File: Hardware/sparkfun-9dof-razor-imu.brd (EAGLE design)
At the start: 31.8 x 31.8 mm, 57 parts, among them J1 LiPo, J3 USD_CONNECTOR, U1 3.3V, U2 MCP73831, U3 MPU-9250, U4 ATSAMD21G-A, Y1 32.768kHz

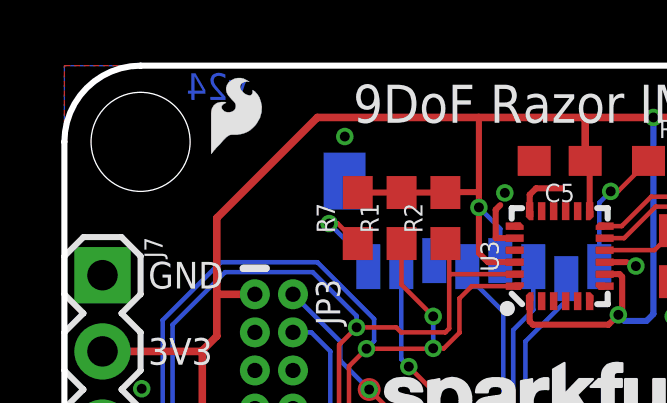
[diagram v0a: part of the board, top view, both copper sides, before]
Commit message: Updating version number to redboard release - v30
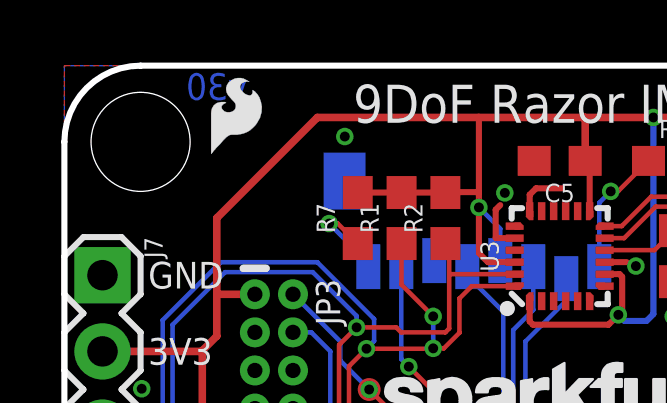
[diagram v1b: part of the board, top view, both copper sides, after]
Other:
- board text added: "v30"
- board text removed: "v24"
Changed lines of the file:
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@@
 <setting verticaltext="up"/>
 </settings>
-<grid distance="0.05" unitdist="inch" unit="inch" style="lines" multiple="1" display="yes" altdistance="0.0025" altunitdist="inch" altunit="inch"/>
+<grid distance="0.05" unitdist="inch" unit="inch" style="lines" multiple="1" display="yes" altdistance="0.005" altunitdist="inch" altunit="inch"/>
 <layers>
 <layer number="1" name="Top" color="4" fill="1" visible="yes" active="yes"/>
@@
 <text x="5.08" y="19.685" size="0.889" layer="22" font="vector" ratio="15" rot="MR0" align="center-left">SDA</text>
 <text x="5.08" y="17.145" size="0.889" layer="22" font="vector" ratio="15" rot="MR0" align="center-left">SCL</text>
-<text x="5.08" y="31.496" size="0.889" layer="16" font="vector" ratio="15" rot="MR180" align="bottom-center">v24</text>
+<text x="5.08" y="31.496" size="0.889" layer="16" font="vector" ratio="15" rot="MR180" align="bottom-center">v30</text>
 <text x="0.254" y="13.97" size="0.889" layer="22" font="vector" ratio="15" rot="MR90" align="bottom-center">ON</text>
 <text x="0.254" y="7.62" size="0.889" layer="22" font="vector" ratio="15" rot="MR90" align="bottom-center">OFF</text>

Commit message: Post-review changes - swapping 3.3V and GND, moving switch in.
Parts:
- moved S1 0.13 mm to (2.92, 10.9)
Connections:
- net 3.3V: now also J5.7; no longer J5.8
- net GND: now also J5.8; no longer J5.7
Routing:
- net 3.3V: track 121.0 -> 123.5 mm
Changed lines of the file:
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@@
 <setting verticaltext="up"/>
 </settings>
-<grid distance="0.05" unitdist="inch" unit="inch" style="lines" multiple="1" display="yes" altdistance="0.005" altunitdist="inch" altunit="inch"/>
+<grid distance="0.05" unitdist="inch" unit="inch" style="lines" multiple="1" display="yes" altdistance="0.001" altunitdist="inch" altunit="inch"/>
 <layers>
 <layer number="1" name="Top" color="4" fill="1" visible="yes" active="yes"/>
@@
 <text x="25.019" y="7.493" size="1.778" layer="22" font="vector" ratio="15" rot="MR0">+</text>
 <text x="20.193" y="7.493" size="1.778" layer="22" font="vector" ratio="15" rot="MR0">-</text>
-<text x="29.0195" y="22.225" size="0.889" layer="21" font="vector" ratio="15" rot="R90" align="bottom-center">GND</text>
-<text x="29.0195" y="24.765" size="0.889" layer="21" font="vector" ratio="15" rot="R90" align="bottom-center">3V3</text>
-<text x="24.13" y="12.065" size="0.889" layer="21" font="vector" ratio="15" align="center-right">A0</text>
+<text x="29.0195" y="24.765" size="0.889" layer="21" font="vector" ratio="15" rot="R90" align="bottom-center">GND</text>
+<text x="29.0195" y="22.225" size="0.889" layer="21" font="vector" ratio="15" rot="R90" align="bottom-center">3V3</text>
+<text x="24.13" y="12.065" size="0.8636" layer="21" font="vector" ratio="15" align="center-right">A0</text>
 <text x="24.13" y="14.605" size="0.889" layer="21" font="vector" ratio="15" align="center-right">A1</text>
 <text x="24.13" y="17.145" size="0.889" layer="21" font="vector" ratio="15" align="center-right">A2</text>
@@
 <text x="20.32" y="2.794" size="0.889" layer="21" font="vector" ratio="15" align="bottom-center">GND</text>
 <text x="23.622" y="2.794" size="0.889" layer="21" font="vector" ratio="15" align="bottom-center">VBAT</text>
-<text x="29.21" y="24.765" size="0.889" layer="22" font="vector" ratio="15" rot="MR270" align="bottom-center">3V3</text>
-<text x="29.21" y="22.225" size="0.889" layer="22" font="vector" ratio="15" rot="MR270" align="bottom-center">GND</text>
+<text x="29.21" y="22.225" size="0.889" layer="22" font="vector" ratio="15" rot="MR270" align="bottom-center">3V3</text>
+<text x="29.21" y="24.765" size="0.889" layer="22" font="vector" ratio="15" rot="MR270" align="bottom-center">GND</text>
 <text x="29.21" y="19.685" size="0.889" layer="22" font="vector" ratio="15" rot="MR270" align="bottom-center">RX</text>
 <text x="29.21" y="17.145" size="0.889" layer="22" font="vector" ratio="15" rot="MR270" align="bottom-center">TX</text>
@@
 <element name="H4" library="SparkFun-Electromechanical" package="STAND-OFF" value="STAND-OFF" x="2.54" y="29.21"/>
 <element name="H3" library="SparkFun-Electromechanical" package="STAND-OFF" value="STAND-OFF" x="29.21" y="29.21"/>
-<element name="S1" library="SparkFun-Electromechanical" package="SWITCH-SPST-SMD-A" value="" x="2.794" y="10.922" rot="MR270">
-<attribute name="PROD_ID" value="SWCH-10651" x="2.794" y="10.922" size="1.778" layer="28" font="vector" ratio="15" rot="MR270" display="off"/>
+<element name="S1" library="SparkFun-Electromechanical" package="SWITCH-SPST-SMD-A" value="" x="2.921" y="10.922" rot="MR270">
+<attribute name="PROD_ID" value="SWCH-10651" x="2.921" y="10.922" size="1.778" layer="28" font="vector" ratio="15" rot="MR270" display="off"/>
 </element>
 <element name="R6" library="SparkFun-Resistors" package="0603" value="100k" x="20.32" y="28.575">
@@
 <via x="5.6261" y="15.2654" extent="1-16" drill="0.3302"/>
 <via x="12.192" y="12.5222" extent="1-16" drill="0.3302"/>
-<contactref element="J5" pad="7"/>
 <via x="22.1996" y="14.6431" extent="1-16" drill="0.3302"/>
 <via x="18.2626" y="13.4874" extent="1-16" drill="0.3302"/>
@@
 <wire x1="18.1864" y1="15.2146" x2="18.7198" y2="15.748" width="0.2032" layer="1"/>
 <wire x1="18.7198" y1="15.748" x2="19.304" y2="15.748" width="0.2032" layer="1"/>
+<contactref element="J5" pad="8"/>
 </signal>
 <signal name="REGOUT">
@@
 <wire x1="4.5974" y1="22.2504" x2="5.08" y2="22.733" width="0.254" layer="1"/>
 <wire x1="1.27" y1="22.225" x2="4.5974" y2="22.225" width="0.254" layer="1"/>
-<contactref element="J5" pad="8"/>
 <wire x1="21.8598" y1="11.815" x2="21.8948" y2="11.85" width="0.254" layer="1"/>
 <wire x1="21.59" y1="30.0228" x2="25.2222" y2="30.0228" width="0.254" layer="1"/>
-<wire x1="25.2222" y1="30.0228" x2="30.48" y2="24.765" width="0.254" layer="1"/>
 <wire x1="15.99" y1="7.815" x2="15.99" y2="6.401" width="0.254" layer="1"/>
 <wire x1="15.99" y1="6.401" x2="16.676" y2="5.715" width="0.254" layer="1"/>
@@
 <wire x1="15.99" y1="17.3108" x2="16.295" y2="17.6158" width="0.254" layer="1"/>
 <wire x1="16.295" y1="17.6158" x2="16.295" y2="19.05" width="0.254" layer="1"/>
+<contactref element="J5" pad="7"/>
+<wire x1="25.2222" y1="30.0228" x2="27.94" y2="27.305" width="0.254" layer="1"/>
+<wire x1="27.94" y1="27.305" x2="27.94" y2="24.765" width="0.254" layer="1"/>
+<wire x1="30.48" y1="22.225" x2="27.94" y2="24.765" width="0.254" layer="1"/>
 </signal>
 <signal name="VDDCORE">
@@
 <wire x1="11.4601" y1="9.84" x2="11.4601" y2="11.6529" width="0.4064" layer="16"/>
 <contactref element="D2" pad="A"/>
-<wire x1="4.544" y1="13.172" x2="4.6101" y2="13.2381" width="0.3048" layer="16"/>
 <wire x1="11.4601" y1="11.6529" x2="11.4601" y2="13.2541" width="0.4064" layer="16"/>
 <wire x1="13.716" y1="11.56" x2="13.7698" y2="11.5062" width="0.4064" layer="16"/>
@@
 <wire x1="8.421" y1="13.6906" x2="7.1374" y2="13.6906" width="0.254" layer="16"/>
 <wire x1="7.1374" y1="13.6906" x2="6.604" y2="14.224" width="0.254" layer="16"/>
-<wire x1="4.6101" y1="13.2381" x2="4.9831" y2="13.2381" width="0.254" layer="16"/>
-<wire x1="4.9831" y1="13.2381" x2="5.969" y2="14.224" width="0.254" layer="16"/>
-<wire x1="5.969" y1="14.224" x2="6.604" y2="14.224" width="0.254" layer="16"/>
+<wire x1="6.0706" y1="14.224" x2="6.604" y2="14.224" width="0.254" layer="16"/>
 <via x="19.6342" y="5.3848" extent="1-16" drill="0.3302"/>
 <wire x1="19.6342" y1="4.3942" x2="16.51" y2="1.27" width="0.4064" layer="1"/>
@@
 <wire x1="19.6342" y1="5.3848" x2="19.2024" y2="5.8166" width="0.4064" layer="16"/>
 <wire x1="19.2024" y1="5.8166" x2="19.2024" y2="10.0076" width="0.4064" layer="16"/>
+<wire x1="6.0706" y1="14.224" x2="5.0186" y2="13.172" width="0.254" layer="16"/>
+<wire x1="5.0186" y1="13.172" x2="4.671" y2="13.172" width="0.254" layer="16"/>
 </signal>
 <signal name="A1">
@@
 <wire x1="10.6782" y1="7.94" x2="9.7282" y2="8.89" width="0.1524" layer="16"/>
 <wire x1="7.0866" y1="11.4046" x2="6.9342" y2="11.557" width="0.1524" layer="16"/>
-<wire x1="6.9342" y1="11.557" x2="4.659" y2="11.557" width="0.1524" layer="16"/>
-<wire x1="4.659" y1="11.557" x2="4.544" y2="11.672" width="0.1524" layer="16"/>
+<wire x1="6.9342" y1="11.557" x2="4.786" y2="11.557" width="0.1524" layer="16"/>
+<wire x1="4.786" y1="11.557" x2="4.671" y2="11.672" width="0.1524" layer="16"/>
 <wire x1="11.4601" y1="7.94" x2="10.6782" y2="7.94" width="0.1524" layer="16"/>
 <wire x1="9.7282" y1="8.89" x2="7.8359" y2="8.89" width="0.1524" layer="16"/>
